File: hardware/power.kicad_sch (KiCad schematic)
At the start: 18 parts, among them U2 AOZ1280CI, U3 LM1117-5.0, U4 LM1117-3.3

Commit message: Release v1.0.0
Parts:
- C13: renamed from C32; value 100nF -> 1μF
- renumbered C9 to C10, C31 to C11, C11 to C12, C12 to C14, C13 to C15, C14 to C16, C15 to C17, C10 to C9
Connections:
- net 6.42V renamed +6.42V
- net PWR+ renamed +24V
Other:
- moved on the sheet: C10, C11, C12, C13, C14, C15, C16, C17, C9, D1, F1, L1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

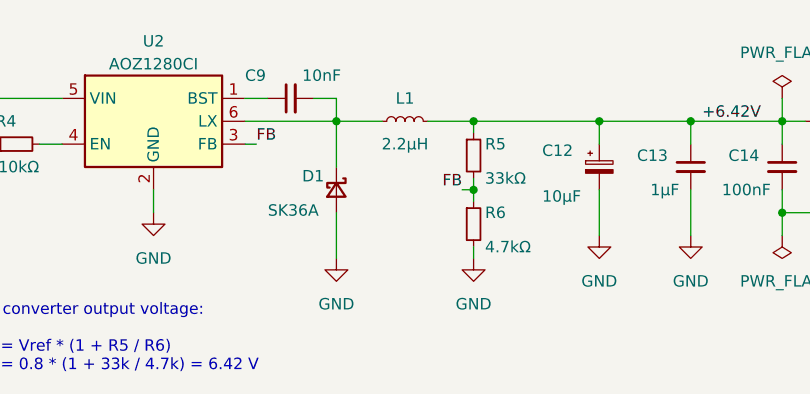
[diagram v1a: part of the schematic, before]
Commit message: Port the project to KiCad 7
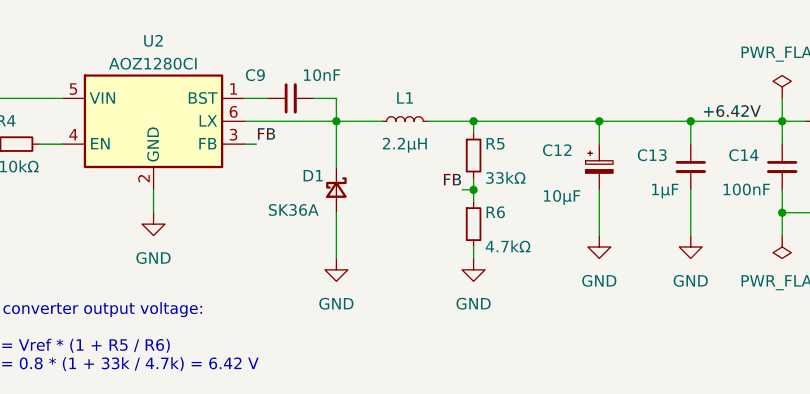
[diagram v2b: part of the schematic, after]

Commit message: Apply KiCad template to the project
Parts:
- U3: symbol Regulator_Linear:LM1117-5.0 -> Regulator_Linear:LM1117MP-5.0
- U4: symbol Regulator_Linear:LM1117-3.3 -> Regulator_Linear:LM1117MP-3.3
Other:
- moved on the sheet: C10, C11, F1, R4

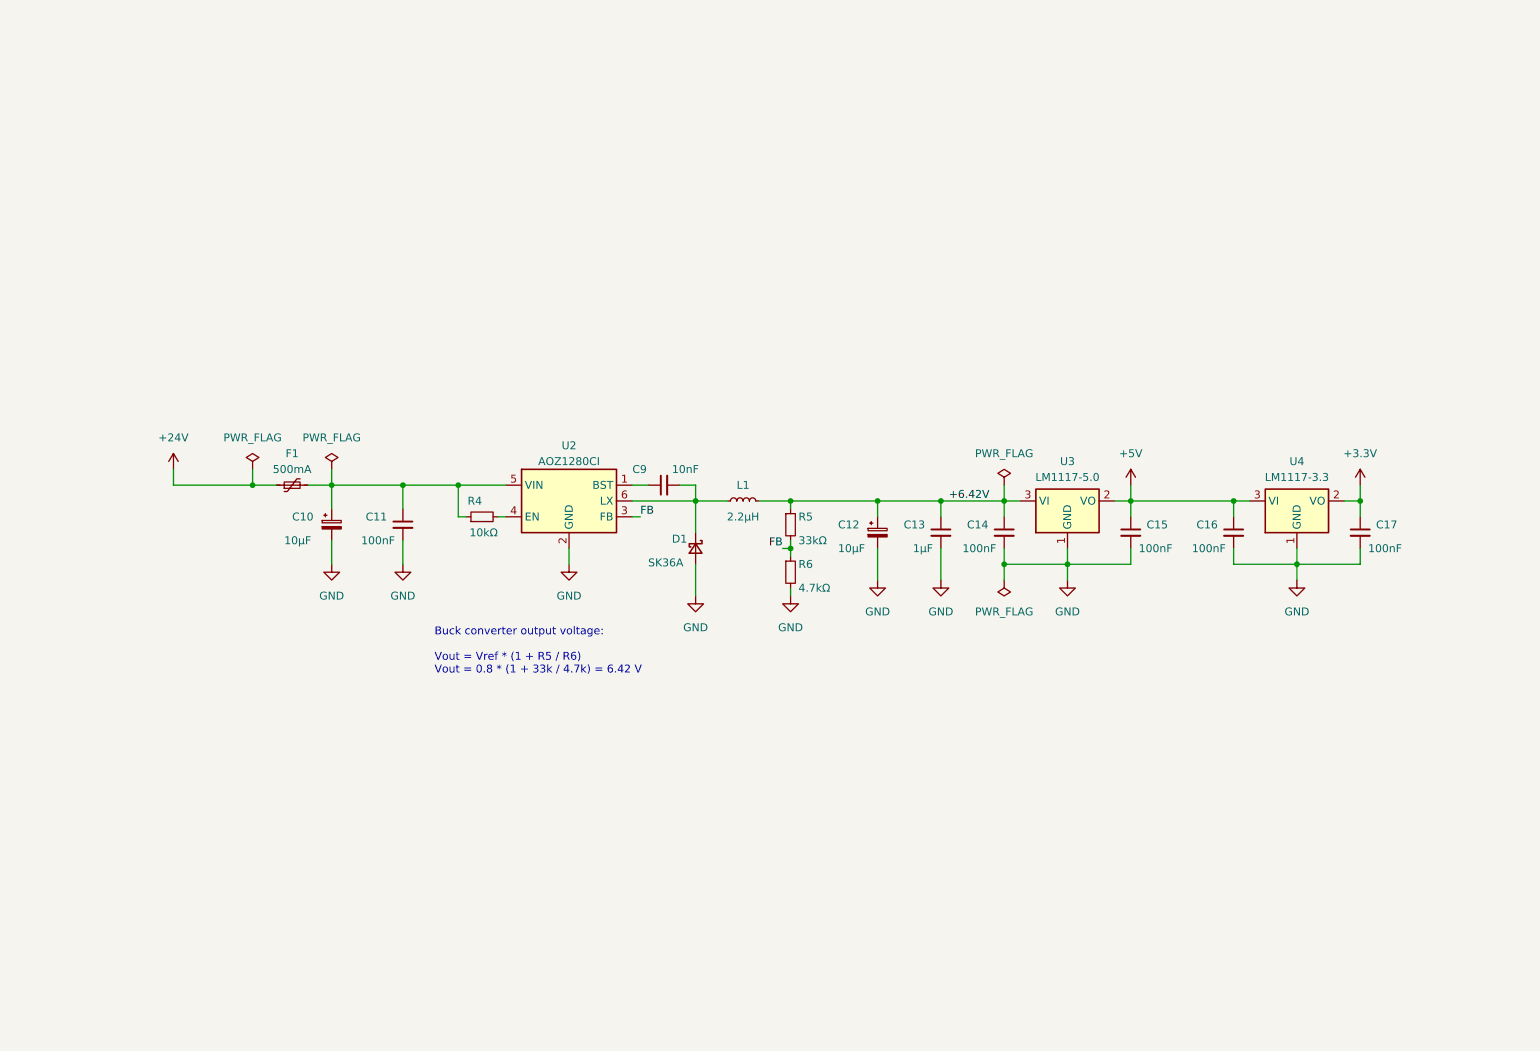
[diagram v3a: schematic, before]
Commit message: Added new, debugged power supply, but the old one is still there, just in case
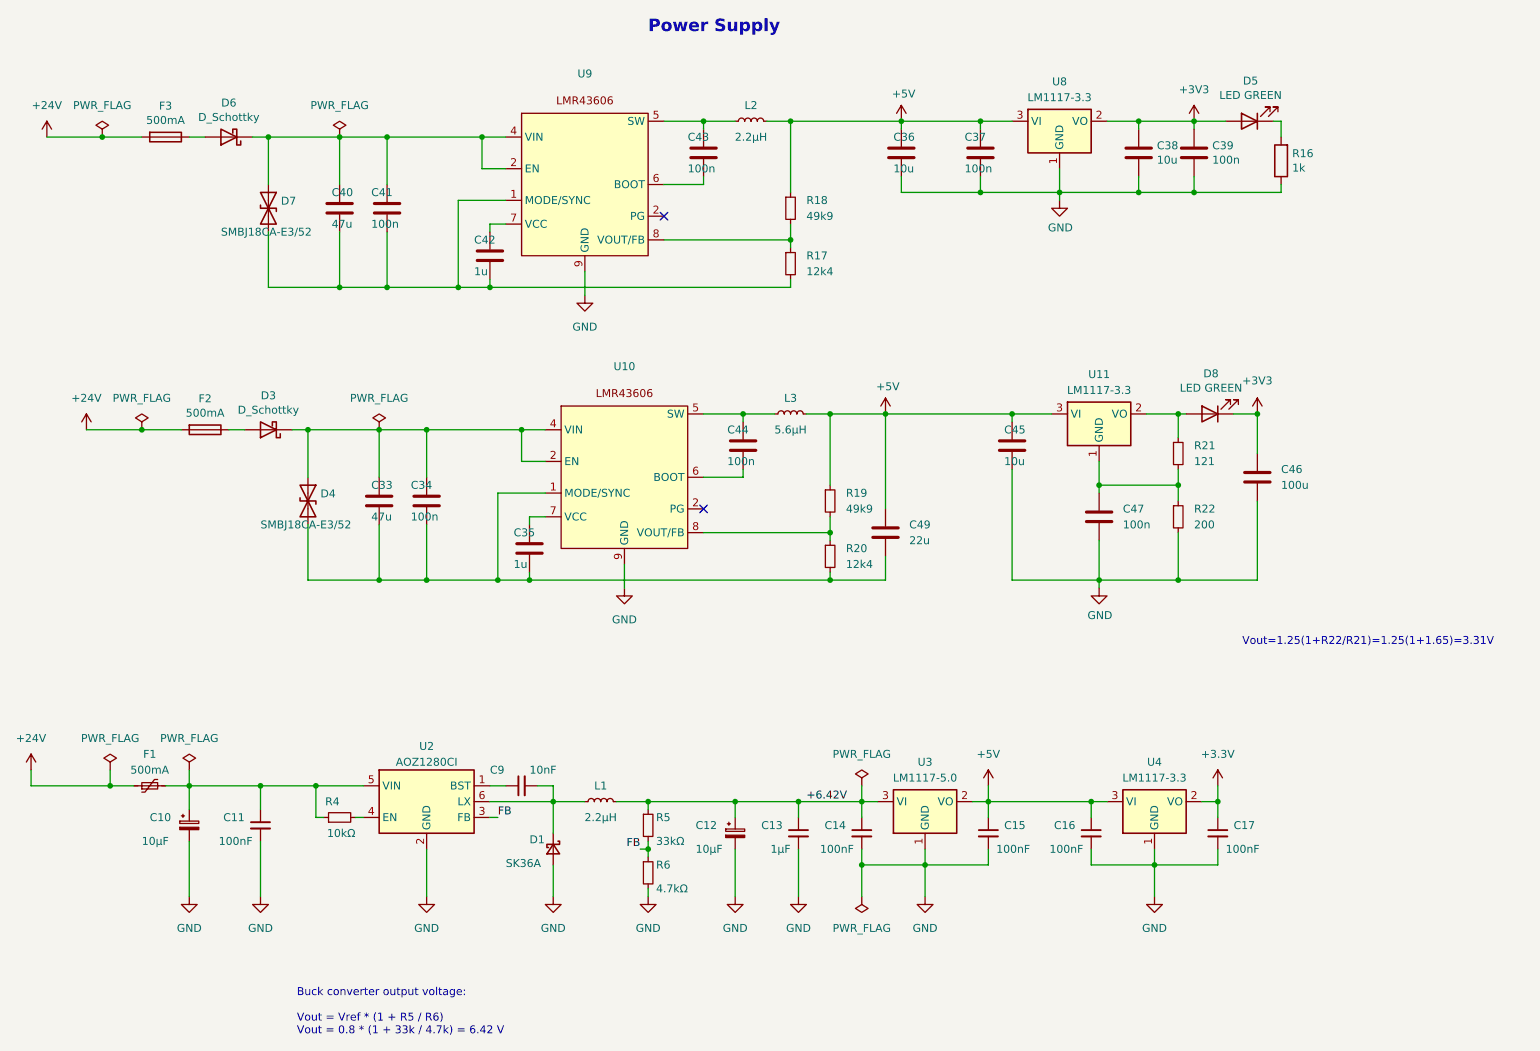
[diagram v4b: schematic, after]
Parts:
- added C33, C40: 47u, Capacitor_SMD:C_1206_3216Metric, symbol Device:C
- added C34, C37, C39, C41, C43, C44: 100n, Capacitor_SMD:C_1206_3216Metric, symbol Device:C
- added C35, C42: 1u, Capacitor_SMD:C_1206_3216Metric, symbol Device:C
- added C36, C38, C45: 10u, Capacitor_SMD:C_1206_3216Metric, symbol Device:C
- added C46: 100u, symbol Device:C
- added C47: 100n, symbol Device:C
- added C49: 22u, symbol Device:C
- added D3, D6: D_Schottky, Diode_SMD:D_SMB, symbol Device:D_Schottky
- added D4, D7: SMBJ18CA-E3/52, Diode_SMD:D_SMB, symbol Device:D_TVS
- added D5, D8: LED GREEN, LED_SMD:LED_PLCC-2, symbol Device:LED
- added F2, F3: 500mA, Fuse:Fuse_1206_3216Metric, symbol Device:Fuse
- added L2: 2.2μH, Inductor_SMD:L_Bourns-SRN4018, symbol Device:L_Small
- added L3: 5.6μH, Inductor_SMD:L_Bourns-SRN4018, symbol Device:L_Small
- added R16: 1k, Resistor_SMD:R_1206_3216Metric, symbol Device:R
- added R17, R20: 12k4, symbol Device:R_Small
- added R18, R19: 49k9, symbol Device:R_Small
- added R21: 121, symbol Device:R_Small
- added R22: 200, symbol Device:R_Small
- added U10, U9: ~, symbol step_down_converter:LMR43606
- added U11, U8: LM1117-3.3, Package_TO_SOT_SMD:SOT-223-3_TabPin2, symbol Regulator_Linear:LM1117MP-3.3
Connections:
- net +24V: now also F2.2, F3.2
- net +5V: now also C36.1, C37.1, C45.1, C49.1, L2.2, L3.2, R18.1, R19.1, U11.3 (VI), U8.3 (VI)
- net GND: now also C36.2, C37.2, C38.2, C39.2, C45.2, C46.2, C47.2, R16.1, R22.2, U10.9 (GND), U8.1 (GND), U9.9 (GND)
- new net: R19.2, R20.1, U10.8 (VOUT/FB)
- new net: D5.1 (K), R16.2
- new net: C33.1, C34.1, D3.1 (K), D4.1 (A1), U10.2 (PG), U10.4 (VIN)
- new net: C33.2, C34.2, C35.2, C49.2, D4.2 (A2), R20.2, U10.1 (MODE/SYNC)
- new net: D3.2 (A), F2.1
- new net: D6.2 (A), F3.1
- new net: C40.1, C41.1, D6.1 (K), D7.1 (A1), U9.2 (PG), U9.4 (VIN)
- new net: C40.2, C41.2, C42.2, D7.2 (A2), R17.2, U9.1 (MODE/SYNC)
- new net: C44.1, L3.1, U10.5 (SW)
- new net: C44.2, U10.6 (BOOT)
- new net: C35.1, U10.7 (VCC)
- new net: C43.1, L2.1, U9.5 (SW)
- new net: D8.2 (A), R21.1, U11.2 (VO)
- new net: C47.1, R21.2, R22.1, U11.1 (GND)
- new net: C43.2, U9.6 (BOOT)
- new net: C42.1, U9.7 (VCC)
- new net: R17.1, R18.2, U9.8 (VOUT/FB)
- new net +3V3: C38.1, C39.1, C46.1, D5.2 (A), D8.1 (K), U8.2 (VO)
- no-connect marks 0 -> 2
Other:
- note added: "Power Supply"
- note added: "Vout=1.25(1+R22/R21)=1.25(1+1.65)=3.31V"
- moved on the sheet: C10, C11, C12, C13, C14, C15, C16, C17, C9, D1, F1, L1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

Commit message: finalna wersja zasilania, zatwierdzona
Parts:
- removed C10, C12: 10μF, Capacitor_SMD:CP_Elec_6.3x5.4, symbol Device:C_Polarized_Small
- removed C11, C14, C15, C16, C17: 100nF, Capacitor_SMD:C_0603_1608Metric, symbol Device:C_Small
- removed C13: 1μF, Capacitor_SMD:C_0603_1608Metric, symbol Device:C_Small
- removed C33: 47u, Capacitor_SMD:C_1206_3216Metric, symbol Device:C
- removed C34, C39, C44: 100n, Capacitor_SMD:C_1206_3216Metric, symbol Device:C
- removed C35: 1u, Capacitor_SMD:C_1206_3216Metric, symbol Device:C
- removed C38, C45: 10u, Capacitor_SMD:C_1206_3216Metric, symbol Device:C
- removed C46: 100u, symbol Device:C
- removed C47: 100n, symbol Device:C
- removed C49: 22u, symbol Device:C
- removed C9: 10nF, Capacitor_SMD:C_0603_1608Metric, symbol Device:C_Small
- removed D1: SK36A, Diode_SMD:D_SMA, symbol Device:D_Schottky_Small
- removed D3: D_Schottky, Diode_SMD:D_SMB, symbol Device:D_Schottky
- removed D4: SMBJ18CA-E3/52, Diode_SMD:D_SMB, symbol Device:D_TVS
- removed D8: LED GREEN, LED_SMD:LED_PLCC-2, symbol Device:LED
- removed F1: 500mA, Fuse:Fuse_0805_2012Metric, symbol Device:Polyfuse_Small
- removed F2: 500mA, Fuse:Fuse_1206_3216Metric, symbol Device:Fuse
- removed L1: 2.2μH, Inductor_SMD:L_Bourns-SRN4018, symbol Device:L_Small
- removed L3: 5.6μH, Inductor_SMD:L_Bourns-SRN4018, symbol Device:L_Small
- removed R19: 49k9, symbol Device:R_Small
- removed R20: 12k4, symbol Device:R_Small
- removed R21: 121, symbol Device:R_Small
- removed R22: 200, symbol Device:R_Small
- removed R4: 10kΩ, Resistor_SMD:R_0603_1608Metric, symbol Device:R_Small
- removed R5: 33kΩ, Resistor_SMD:R_0603_1608Metric, symbol Device:R_Small
- removed R6: 4.7kΩ, Resistor_SMD:R_0603_1608Metric, symbol Device:R_Small
- removed U10: ~, symbol step_down_converter:LMR43606
- removed U11, U4: LM1117-3.3, Package_TO_SOT_SMD:SOT-223-3_TabPin2, symbol Regulator_Linear:LM1117MP-3.3
- removed U2: AOZ1280CI, Package_TO_SOT_SMD:SOT-23-6, symbol Regulator_Switching:AOZ1280CI
- removed U3: LM1117-5.0, Package_TO_SOT_SMD:SOT-223-3_TabPin2, symbol Regulator_Linear:LM1117MP-5.0
- added C39: 50u, symbol Device:C_Polarized_Small
- C40: value 47u -> 4u7
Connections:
- net +3V3: now also C39.1
- net GND: now also C40.2, C41.2, C42.2, D7.2 (A2), R17.2, U9.1 (MODE/SYNC), C39.2
- no-connect marks 2 -> 1
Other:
- note removed: "Buck converter output voltage: Vout = Vref * (1 + R5 / R6) Vout = 0.8 * (1 + 33k / 4.7k) = 6.42 V"
- note removed: "Vout=1.25(1+R22/R21)=1.25(1+1.65)=3.31V"
- moved on the sheet: C36, C37, C40, C41, C42, C43, D5, D6, D7, F3, L2, R16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
